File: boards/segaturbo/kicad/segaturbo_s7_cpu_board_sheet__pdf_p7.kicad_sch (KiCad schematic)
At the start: 19 parts, among them IC1 2716, IC13 2716, IC14 2716, IC15 74LS283, IC16 74LS283, IC2 2716, IC27 2716, IC28 2716, IC29 74LS283, IC3 74LS283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

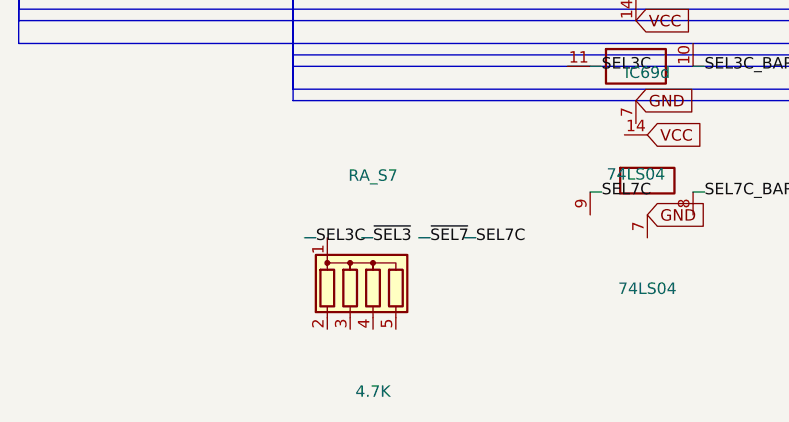
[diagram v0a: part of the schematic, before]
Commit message: Fix KiCad pin-aligned generated symbols
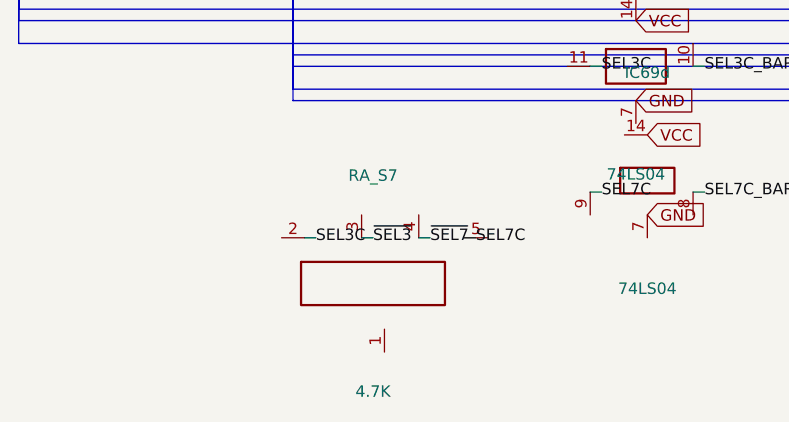
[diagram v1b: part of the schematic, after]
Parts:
- RA_S7: symbol Device:R_Network04 -> user:_chip_RA_S7
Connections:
- net SEL3C: now also RA_S7.2
- net SEL7C: now also RA_S7.5
- net ~{SEL3}: now also RA_S7.3
- net ~{SEL7}: now also RA_S7.4
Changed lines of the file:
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@@
   )
   (symbol
-    (lib_id "Device:R_Network04")
+    (lib_id "user:_chip_RA_S7")
     (at 106.68 227.33 0)
     (unit 1)
